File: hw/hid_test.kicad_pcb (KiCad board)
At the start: 2 copper layers, 175.3 x 111.5 mm, 125 parts, among them J1 USB_B_Micro, J10 TWI, J2 2x8 Connector, J3 ISP, J4 2x8 Connector, J5 2x8, J6 ILI9163, J7 ILI9163, J8 ILI9163, J9 ILI9163, Q1 2N3904, SW1 SW_Push, U1 ATmega644-20PU, U2 CD4555BE, U3 LD1117S33TR, Y1 20MHz

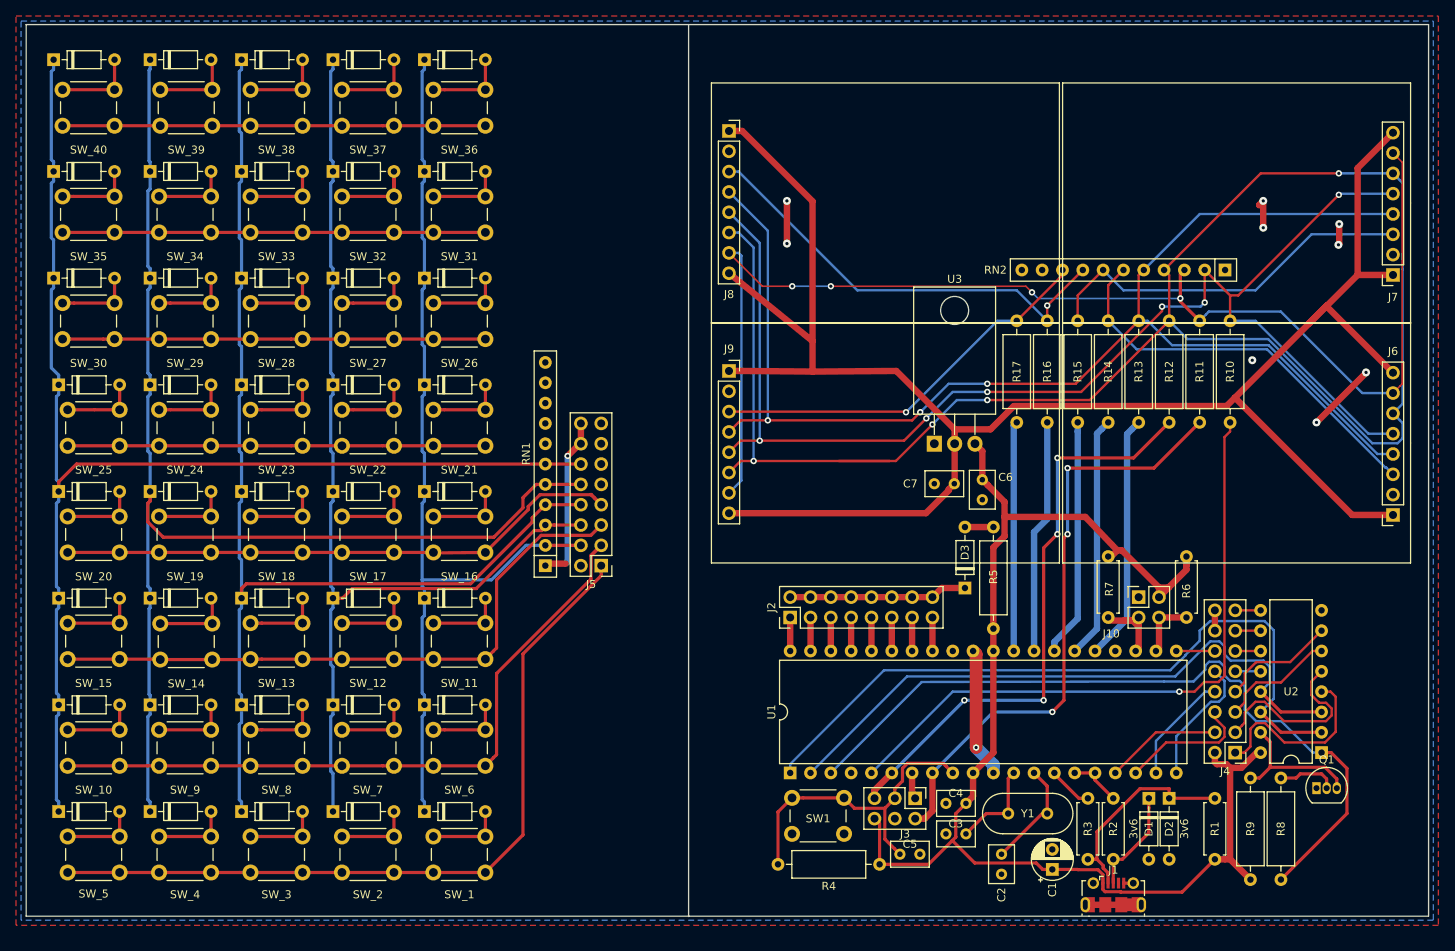
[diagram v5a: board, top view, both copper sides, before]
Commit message: Little adjustments and added mounting holes
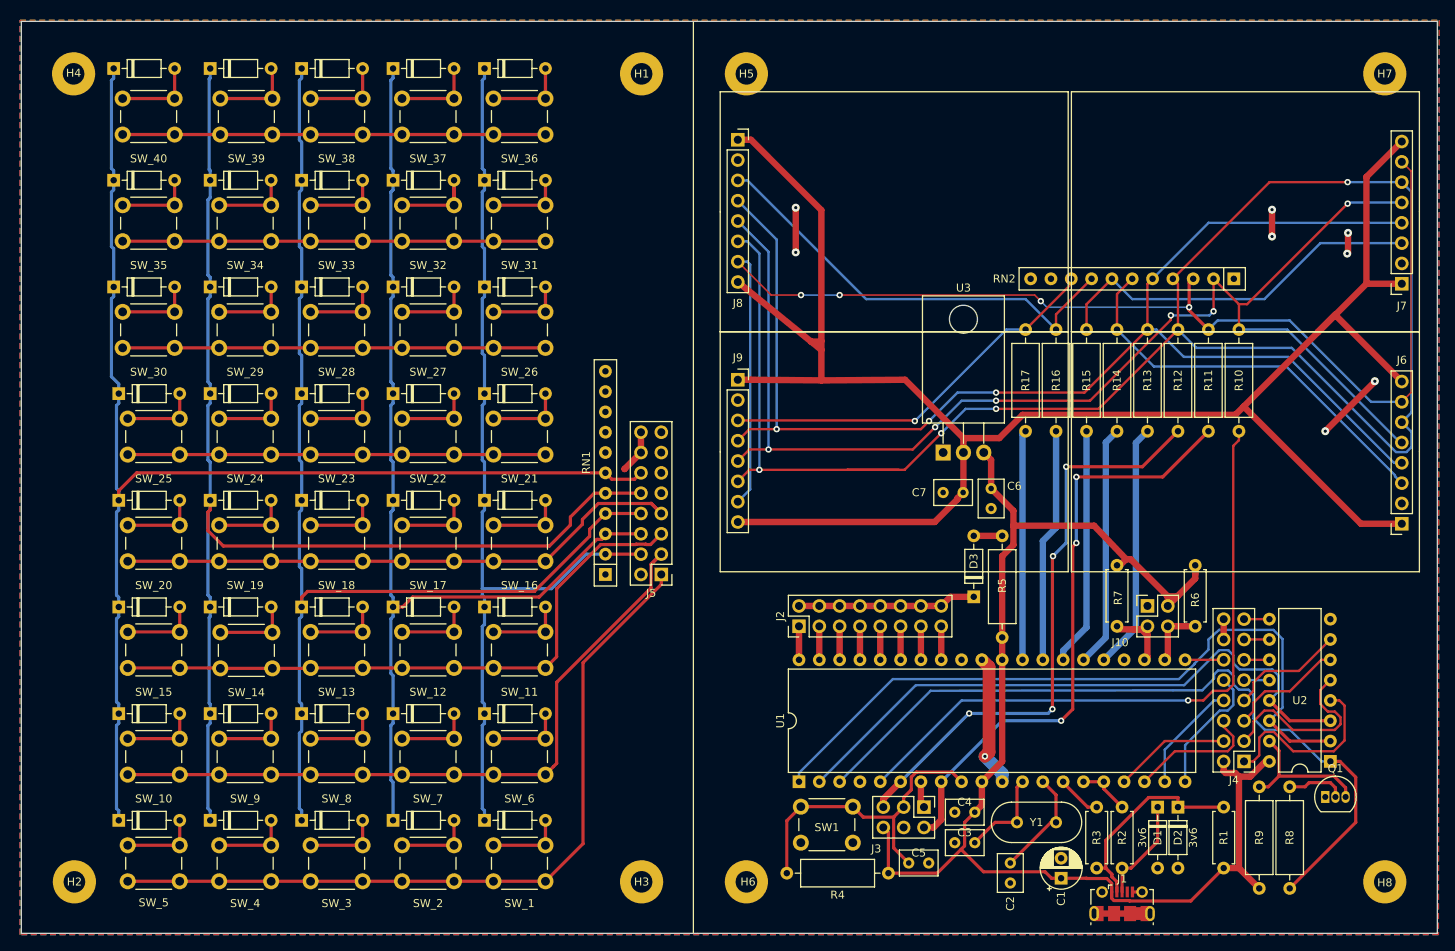
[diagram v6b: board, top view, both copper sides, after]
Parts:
- added H1: Hole, MountingHole:MountingHole_2.7mm_M2.5_Pad, F.Cu at (89.6, 18.7)
- added H2: Hole, MountingHole:MountingHole_2.7mm_M2.5_Pad, F.Cu at (18.7, 119.7)
- added H3: Hole, MountingHole:MountingHole_2.7mm_M2.5_Pad, F.Cu at (89.6, 119.7)
- added H4: Hole, MountingHole:MountingHole_2.7mm_M2.5_Pad, F.Cu at (18.6, 18.7)
- added H5: Hole, MountingHole:MountingHole_2.7mm_M2.5_Pad, F.Cu at (102.7, 18.7)
- added H6: Hole, MountingHole:MountingHole_2.7mm_M2.5_Pad, F.Cu at (102.7, 119.7)
- added H7: Hole, MountingHole:MountingHole_2.7mm_M2.5_Pad, F.Cu at (182.5, 18.7)
- added H8: Hole, MountingHole:MountingHole_2.7mm_M2.5_Pad, F.Cu at (182.5, 119.7)
- moved D13 7.59 mm to (50.9, 101.2)
- moved D17 7.59 mm to (39.5, 101.2)
- moved D5 7.59 mm to (73.8, 101.2)
- moved D9 7.59 mm to (62.4, 101.2)
- moved SW_11 7.59 mm to (77.6, 92.9)
- moved SW_21 7.59 mm to (77.6, 66.3)
- moved D24 7.59 mm to (73.8, 61.2)
- moved D25 7.59 mm to (73.8, 47.8)
- moved D27 7.59 mm to (73.8, 20.5)
- moved D28 7.59 mm to (62.4, 61.2)
- moved D29 7.59 mm to (62.4, 47.8)
- moved D31 7.59 mm to (62.4, 20.5)
- moved D32 7.59 mm to (50.9, 61.2)
- moved D33 7.59 mm to (50.9, 47.8)
- moved D35 7.59 mm to (50.9, 20.5)
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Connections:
- J5 pad 2: +5V -> (no net)
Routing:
- net GND: track 68.3 -> 53.0 mm, vias 10 -> 9
- net +3V3: track 239.8 -> 241.2 mm
- net MatrixBoard_Row_4: track 71.1 -> 72.4 mm
- net Switch_Matrix_E: track 163.3 -> 163.9 mm
- net (no net): track 0.05 -> 0.00 mm, vias 1 -> 0
- net SPI_~SS: vias 2 -> 1
- net DISPLAY_SEL_3_3v3: vias 1 -> 0
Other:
- board size 175.3 x 111.5 mm -> 177 x 114 mm
